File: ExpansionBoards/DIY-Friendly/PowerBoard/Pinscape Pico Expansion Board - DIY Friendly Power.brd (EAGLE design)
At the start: 138 x 100 mm, 87 parts, among them IC1 UCC27524P, IC10 ULN2803A, IC11 ULN2803A, IC12 ULN2803A, IC13 DS1307+, IC2 UCC27524P, IC3 UCC27524P, IC4 UCC27524P, IC5 UCC27524P, IC6 UCC27524P, IC7 UCC27524P, IC8 UCC27524P, IC9 ULN2803A, J1 640445-9, J2 640445-9, J3 640445-6, J4 1-640456-0, J5 1-640456-0, J6 1-640456-0, J7 1-640456-0, Q1 FDPF085N10A, Q10 FDPF085N10A, Q11 FDPF085N10A, Q12 FDPF085N10A, Q13 FDPF085N10A, Q14 FDPF085N10A, Q15 FDPF085N10A, Q16 FDPF085N10A, Q17 2N2222A, Q18 2N2222A, Q2 FDPF085N10A, Q3 FDPF085N10A, Q4 FDPF085N10A, Q5 FDPF085N10A, Q6 FDPF085N10A, Q7 FDPF085N10A, Q8 FDPF085N10A, Q9 FDPF085N10A, Y1 ECS-.327-12.5-13X-C

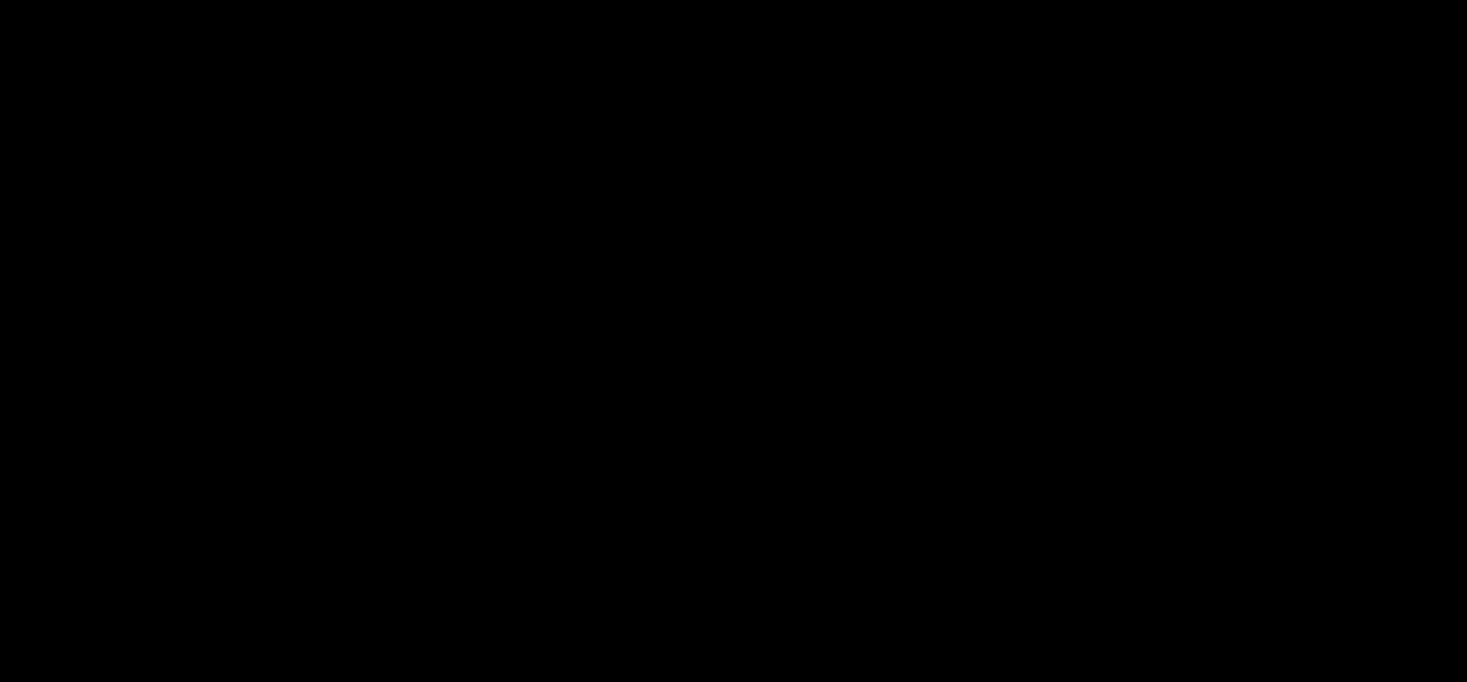
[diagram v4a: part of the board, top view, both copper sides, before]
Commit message: KL25Z adapters - connect AGND to GND
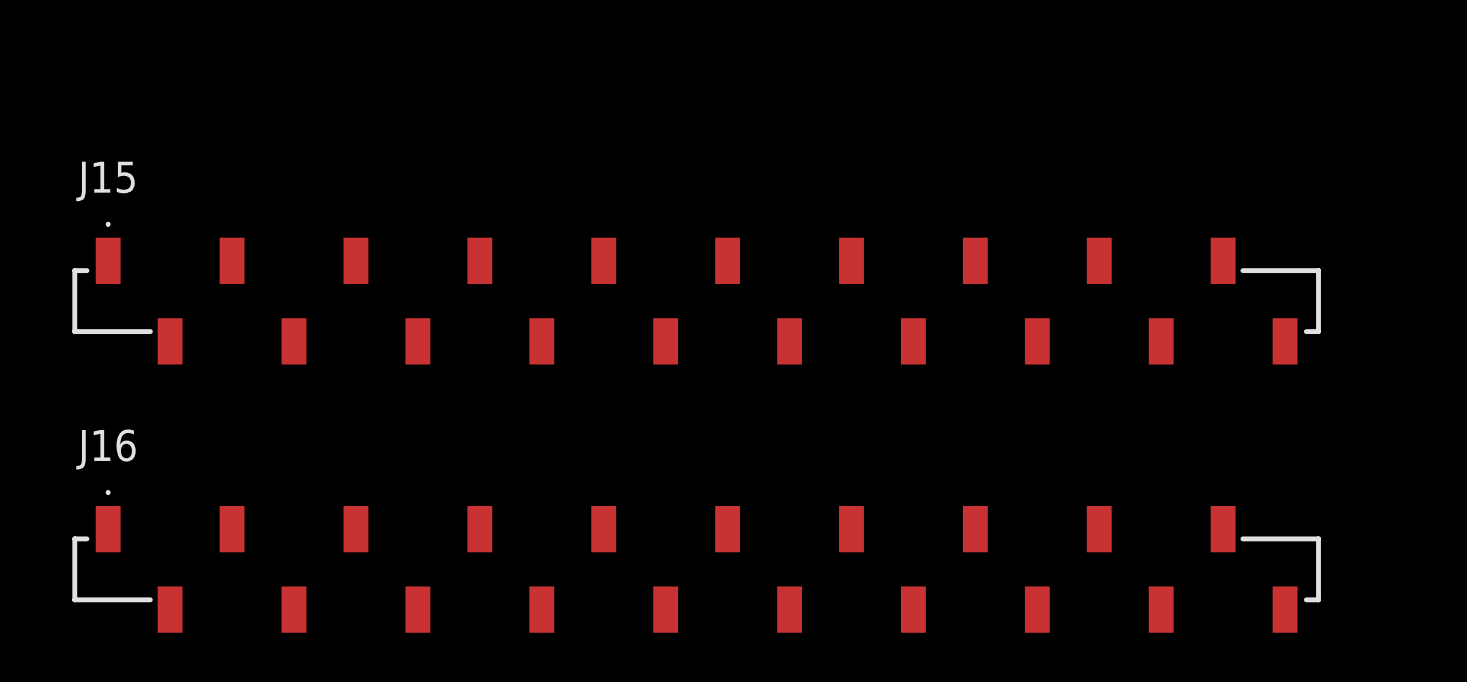
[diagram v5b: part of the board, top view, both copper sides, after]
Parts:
- added J15, J16: M20-7862042B, SamacSys_Parts:M20-7862042-B
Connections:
- net GND: now also J15.13, J15.18, J15.3, J15.8, J16.13, J16.18, J16.3, J16.8
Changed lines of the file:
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@@
 <attribute name="VALUE" x="17.18" y="39.152" size="1.27" layer="27" ratio="10" rot="R90"/>
 </element>
+<element name="J15" library="SamacSys_Parts" package="M20-7862042-B" value="M20-7862042B" x="20.1" y="-13.4"/>
+<element name="J16" library="SamacSys_Parts" package="M20-7862042-B" value="M20-7862042B" x="20.1" y="-24.4"/>
 </elements>
 <signals>
@@
 <contactref element="S1" pad="2"/>
 <contactref element="S1" pad="1"/>
+<contactref element="J15" pad="3"/>
+<contactref element="J15" pad="8"/>
+<contactref element="J15" pad="18"/>
+<contactref element="J16" pad="18"/>
+<contactref element="J16" pad="13"/>
+<contactref element="J16" pad="8"/>
+<contactref element="J16" pad="3"/>
+<contactref element="J15" pad="13"/>
+<wire x1="113.72" y1="93.7" x2="117.68" y2="93.7" width="0" layer="19" extent="1-1"/>
+<wire x1="109.76" y1="93.7" x2="113.72" y2="93.7" width="0" layer="19" extent="1-1"/>
+<wire x1="105.8" y1="93.7" x2="109.76" y2="93.7" width="0" layer="19" extent="1-1"/>
+<wire x1="106.44" y1="83.94" x2="105.8" y2="91.4" width="0" layer="19" extent="16-16"/>
+<wire x1="99.64" y1="83.94" x2="106.44" y2="83.94" width="0" layer="19" extent="1-1"/>
+<wire x1="102.8" y1="78.1" x2="99.64" y2="83.94" width="0" layer="19" extent="1-1"/>
+<wire x1="92.84" y1="83.94" x2="99.64" y2="83.94" width="0" layer="19" extent="1-1"/>
+<wire x1="95.8" y1="78.1" x2="92.84" y2="83.94" width="0" layer="19" extent="1-1"/>
+<wire x1="89.3" y1="78.1" x2="95.8" y2="78.1" width="0" layer="19" extent="1-1"/>
+<wire x1="86.04" y1="83.94" x2="89.3" y2="78.1" width="0" layer="19" extent="1-1"/>
+<wire x1="79.14" y1="83.94" x2="86.04" y2="83.94" width="0" layer="19" extent="1-1"/>
+<wire x1="82.1" y1="78.2" x2="79.14" y2="83.94" width="0" layer="19" extent="1-1"/>
+<wire x1="75.5" y1="78.1" x2="82.1" y2="78.2" width="0" layer="19" extent="1-1"/>
+<wire x1="72.44" y1="83.94" x2="75.5" y2="78.1" width="0" layer="19" extent="1-1"/>
+<wire x1="65.84" y1="83.94" x2="72.44" y2="83.94" width="0" layer="19" extent="1-1"/>
+<wire x1="68.8" y1="78" x2="65.84" y2="83.94" width="0" layer="19" extent="1-1"/>
+<wire x1="62" y1="77.9" x2="68.8" y2="78" width="0" layer="19" extent="1-1"/>
+<wire x1="58.74" y1="83.94" x2="62" y2="77.9" width="0" layer="19" extent="1-1"/>
+<wire x1="51.94" y1="83.94" x2="58.74" y2="83.94" width="0" layer="19" extent="1-1"/>
+<wire x1="55" y1="77.9" x2="51.94" y2="83.94" width="0" layer="19" extent="1-1"/>
+<wire x1="45.14" y1="83.94" x2="51.94" y2="83.94" width="0" layer="19" extent="1-1"/>
+<wire x1="48" y1="77.8" x2="45.14" y2="83.94" width="0" layer="19" extent="1-1"/>
+<wire x1="41.3" y1="77.9" x2="48" y2="77.8" width="0" layer="19" extent="1-1"/>
+<wire x1="38.14" y1="83.94" x2="41.3" y2="77.9" width="0" layer="19" extent="1-1"/>
+<wire x1="31.34" y1="83.94" x2="38.14" y2="83.94" width="0" layer="19" extent="1-1"/>
+<wire x1="34.3" y1="77.9" x2="31.34" y2="83.94" width="0" layer="19" extent="1-1"/>
+<wire x1="24.54" y1="83.94" x2="31.34" y2="83.94" width="0" layer="19" extent="1-1"/>
+<wire x1="17.74" y1="83.94" x2="24.54" y2="83.94" width="0" layer="19" extent="1-1"/>
+<wire x1="11.14" y1="84.04" x2="17.74" y2="83.94" width="0" layer="19" extent="1-1"/>
+<wire x1="4.44" y1="83.94" x2="11.14" y2="84.04" width="0" layer="19" extent="1-1"/>
+<wire x1="7.5" y1="77.8" x2="4.44" y2="83.94" width="0" layer="19" extent="1-1"/>
+<wire x1="14.2" y1="77.8" x2="7.5" y2="77.8" width="0" layer="19" extent="1-1"/>
+<wire x1="21" y1="77.8" x2="14.2" y2="77.8" width="0" layer="19" extent="1-1"/>
+<wire x1="14.5" y1="70.77" x2="14.2" y2="77.8" width="0" layer="19" extent="1-1"/>
+<wire x1="14.5" y1="63.63" x2="14.5" y2="70.77" width="0" layer="19" extent="1-1"/>
+<wire x1="9.17" y1="63.23" x2="14.5" y2="63.63" width="0" layer="19" extent="1-1"/>
+<wire x1="40.9" y1="70.67" x2="41.3" y2="77.9" width="0" layer="19" extent="1-1"/>
+<wire x1="40.9" y1="63.63" x2="40.9" y2="70.67" width="0" layer="19" extent="1-1"/>
+<wire x1="35.57" y1="63.23" x2="40.9" y2="63.63" width="0" layer="19" extent="1-1"/>
+<wire x1="54.1" y1="70.67" x2="55" y2="77.9" width="0" layer="19" extent="1-1"/>
+<wire x1="54.1" y1="63.63" x2="54.1" y2="70.67" width="0" layer="19" extent="1-1"/>
+<wire x1="48.77" y1="63.23" x2="54.1" y2="63.63" width="0" layer="19" extent="1-1"/>
+<wire x1="67.3" y1="70.67" x2="68.8" y2="78" width="0" layer="19" extent="1-1"/>
+<wire x1="67.3" y1="63.63" x2="67.3" y2="70.67" width="0" layer="19" extent="1-1"/>
+<wire x1="61.97" y1="63.23" x2="67.3" y2="63.63" width="0" layer="19" extent="1-1"/>
+<wire x1="80.5" y1="70.67" x2="82.1" y2="78.2" width="0" layer="19" extent="1-1"/>
+<wire x1="80.5" y1="63.63" x2="80.5" y2="70.67" width="0" layer="19" extent="1-1"/>
+<wire x1="75.17" y1="63.23" x2="80.5" y2="63.63" width="0" layer="19" extent="1-1"/>
+<wire x1="93.7" y1="70.67" x2="95.8" y2="78.1" width="0" layer="19" extent="1-1"/>
+<wire x1="93.7" y1="63.63" x2="93.7" y2="70.67" width="0" layer="19" extent="1-1"/>
+<wire x1="88.37" y1="63.23" x2="93.7" y2="63.63" width="0" layer="19" extent="1-1"/>
+<wire x1="101.57" y1="63.23" x2="93.7" y2="63.63" width="0" layer="19" extent="1-1"/>
+<wire x1="106.9" y1="63.63" x2="101.57" y2="63.23" width="0" layer="19" extent="1-1"/>
+<wire x1="106.9" y1="70.67" x2="106.9" y2="63.63" width="0" layer="19" extent="1-1"/>
+<wire x1="27.7" y1="63.63" x2="35.57" y2="63.23" width="0" layer="19" extent="1-1"/>
+<wire x1="22.37" y1="63.23" x2="27.7" y2="63.63" width="0" layer="19" extent="1-1"/>
+<wire x1="27.7" y1="70.67" x2="27.7" y2="63.63" width="0" layer="19" extent="1-1"/>
+<wire x1="117.29" y1="61.14" x2="106.9" y2="63.63" width="0" layer="19" extent="1-1"/>
+<wire x1="76" y1="50.63" x2="75.17" y2="63.23" width="0" layer="19" extent="1-1"/>
+<wire x1="85.525" y1="45.55" x2="76" y2="50.63" width="0" layer="19" extent="1-1"/>
+<wire x1="66.475" y1="45.55" x2="76" y2="50.63" width="0" layer="19" extent="1-1"/>
+<wire x1="58.4394" y1="40.5512" x2="66.475" y2="45.55" width="0" layer="19" extent="1-1"/>
+<wire x1="58.4394" y1="34.0488" x2="58.4394" y2="40.5512" width="0" layer="19" extent="1-1"/>
+<wire x1="66.475" y1="32.85" x2="58.4394" y2="34.0488" width="0" layer="19" extent="1-1"/>
+<wire x1="34.45" y1="50.6" x2="35.57" y2="63.23" width="0" layer="19" extent="1-1"/>
+<wire x1="43.975" y1="45.52" x2="34.45" y2="50.6" width="0" layer="19" extent="1-1"/>
+<wire x1="24.925" y1="45.52" x2="34.45" y2="50.6" width="0" layer="19" extent="1-1"/>
+<wire x1="61.61" y1="21.13" x2="66.475" y2="32.85" width="0" layer="19" extent="1-1"/>
+<wire x1="66.475" y1="20.15" x2="61.61" y2="21.13" width="0" layer="19" extent="1-1"/>
+<wire x1="57.7" y1="9.7" x2="61.61" y2="21.13" width="0" layer="19" extent="1-1"/>
+<wire x1="66.475" y1="7.45" x2="57.7" y2="9.7" width="0" layer="19" extent="1-1"/>
+<wire x1="85.525" y1="32.85" x2="85.525" y2="45.55" width="0" layer="19" extent="1-1"/>
+<wire x1="85.525" y1="20.15" x2="85.525" y2="32.85" width="0" layer="19" extent="1-1"/>
+<wire x1="91.14" y1="19.61" x2="85.525" y2="20.15" width="0" layer="19" extent="1-1"/>
+<wire x1="85.525" y1="7.45" x2="85.525" y2="20.15" width="0" layer="19" extent="1-1"/>
+<wire x1="43.975" y1="32.82" x2="43.975" y2="45.52" width="0" layer="19" extent="1-1"/>
+<wire x1="43.975" y1="20.12" x2="43.975" y2="32.82" width="0" layer="19" extent="1-1"/>
+<wire x1="24.925" y1="32.82" x2="24.925" y2="45.52" width="0" layer="19" extent="1-1"/>
+<wire x1="43.975" y1="7.42" x2="43.975" y2="20.12" width="0" layer="19" extent="1-1"/>
+<wire x1="24.925" y1="20.12" x2="24.925" y2="32.82" width="0" layer="19" extent="1-1"/>
+<wire x1="13.6" y1="18.4" x2="24.925" y2="20.12" width="0" layer="19" extent="1-1"/>
+<wire x1="4.71" y1="24.75" x2="13.6" y2="18.4" width="0" layer="19" extent="1-1"/>
+<wire x1="4.71" y1="29.83" x2="4.71" y2="24.75" width="0" layer="19" extent="1-1"/>
+<wire x1="4.71" y1="34.91" x2="4.71" y2="29.83" width="0" layer="19" extent="1-1"/>
+<wire x1="4.71" y1="39.99" x2="4.71" y2="34.91" width="0" layer="19" extent="1-1"/>
+<wire x1="9.8394" y1="38.9488" x2="4.71" y2="39.99" width="0" layer="19" extent="1-1"/>
+<wire x1="9.8394" y1="45.4512" x2="9.8394" y2="38.9488" width="0" layer="19" extent="1-1"/>
+<wire x1="24.925" y1="7.42" x2="24.925" y2="20.12" width="0" layer="19" extent="1-1"/>
+<wire x1="101.4" y1="36.5" x2="85.525" y2="32.85" width="0" layer="19" extent="1-1"/>
+<wire x1="106.8" y1="45.4" x2="101.4" y2="36.5" width="0" layer="19" extent="1-1"/>
+<wire x1="105.9" y1="27.1" x2="101.4" y2="36.5" width="0" layer="19" extent="1-1"/>
+<wire x1="117.39" y1="37.94" x2="106.8" y2="45.4" width="0" layer="19" extent="1-1"/>
+<wire x1="117.39" y1="14.64" x2="105.9" y2="27.1" width="0" layer="19" extent="1-1"/>
+<wire x1="26.45" y1="-11.75" x2="24.925" y2="7.42" width="0" layer="19" extent="1-1"/>
+<wire x1="26.45" y1="-22.75" x2="26.45" y2="-11.75" width="0" layer="19" extent="1-1"/>
+<wire x1="39.15" y1="-15.05" x2="26.45" y2="-11.75" width="0" layer="19" extent="1-1"/>
+<wire x1="39.15" y1="-26.05" x2="39.15" y2="-15.05" width="0" layer="19" extent="1-1"/>
+<wire x1="13.75" y1="-26.05" x2="26.45" y2="-22.75" width="0" layer="19" extent="1-1"/>
+<wire x1="13.75" y1="-15.05" x2="13.75" y2="-26.05" width="0" layer="19" extent="1-1"/>
+<wire x1="1.05" y1="-22.75" x2="13.75" y2="-26.05" width="0" layer="19" extent="1-1"/>
+<wire x1="1.05" y1="-11.75" x2="1.05" y2="-22.75" width="0" layer="19" extent="1-1"/>
 </signal>
 <signal name="SDA">
